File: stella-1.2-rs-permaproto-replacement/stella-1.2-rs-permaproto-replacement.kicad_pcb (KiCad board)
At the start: 2 copper layers, 81 x 51 mm, 10 parts, among them J1 Conn_01x03, J2 Conn_01x04, U1 Triad, U2 Humidity, U3 Surface Temp, U4 Range

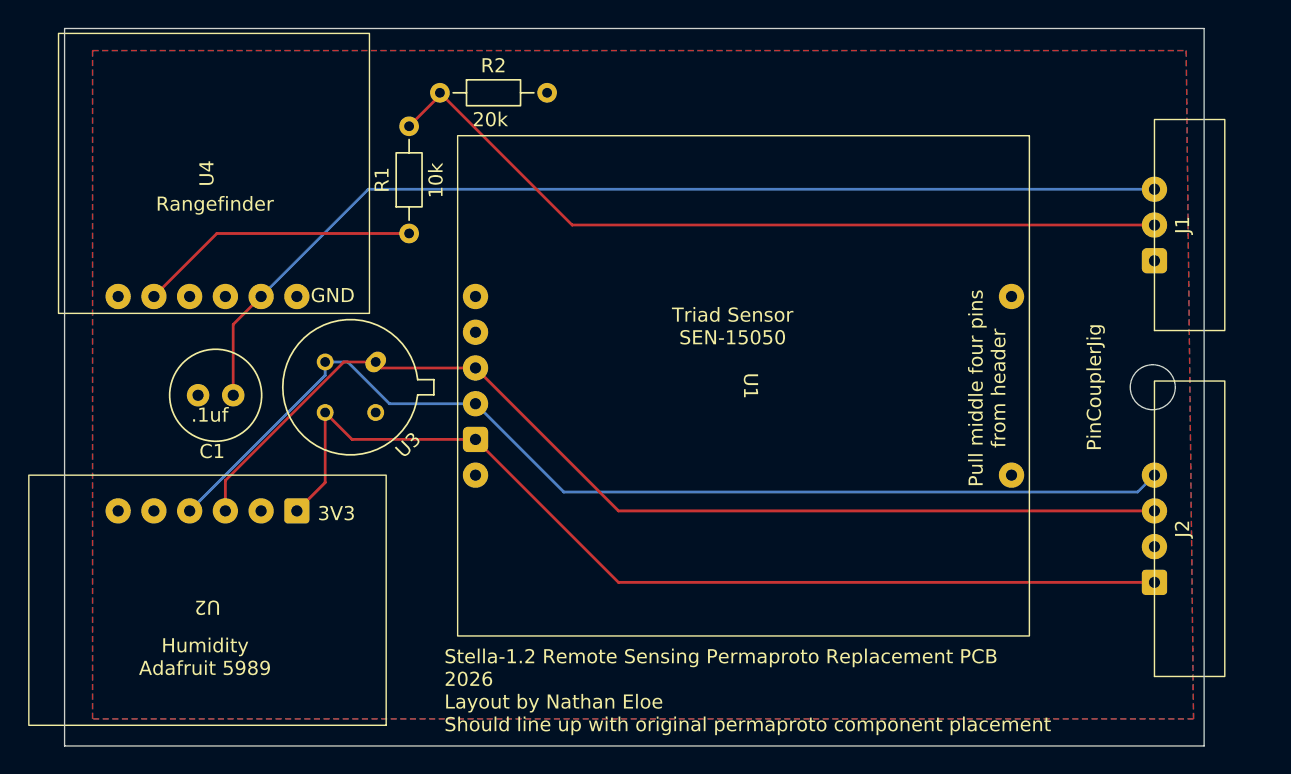
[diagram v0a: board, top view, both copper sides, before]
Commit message: Add RS build fixes (size, pins)
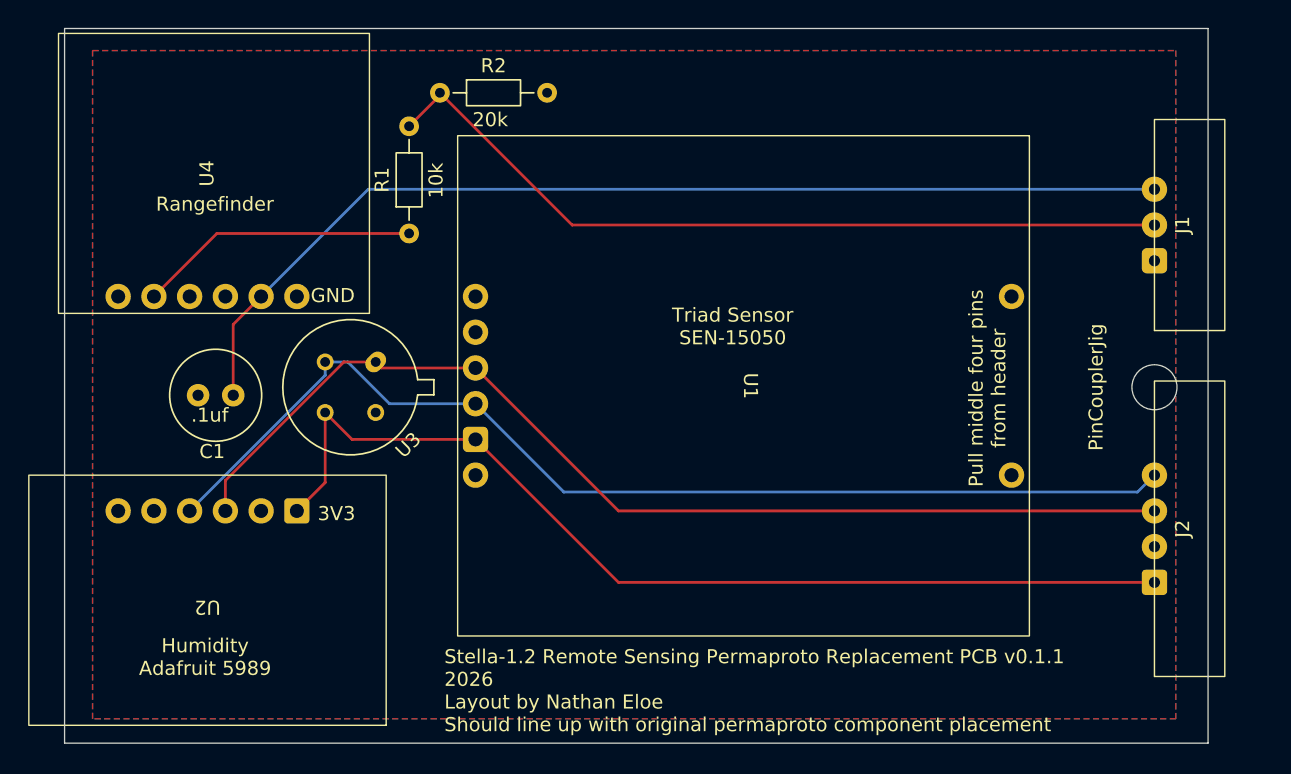
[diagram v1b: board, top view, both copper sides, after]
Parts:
- moved PinCouplerJig 0.12 mm to (157.5, 100.4)
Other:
- board size 81 x 51 mm -> 81.3 x 50.8 mm
- board text added: "Stella-1.2 Remote Sensing Permaproto Replacement PCB v0.1.1 2026 Layout by Nathan Eloe Should line up with original permaproto component placement"
- board text removed: "Stella-1.2 Remote Sensing Permaproto Replacement PCB 2026 Layout by Nathan Eloe Should line up with original permaproto component placement"
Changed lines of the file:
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@@
 		(sheetname "/")
 		(sheetfile "stella-1.2-rs-permaproto-replacement.kicad_sch")
-		(units
-			(unit
-				(name "A")
-				(pins "6" "5" "4" "3" "2" "1" "9" "8" "7")
-			)
-		)
 		(attr smd)
 		(duplicate_pad_numbers_are_jumpers no)
@@
 			(at -6.35 -19.05 270)
 			(size 1.8 1.8)
-			(drill 0.8)
+			(drill 1)
 			(layers "*.Cu" "*.Mask")
 			(remove_unused_layers no)
@@
 			(at 6.35 19.05 270)
 			(size 1.8 1.8)
-			(drill 0.8)
+			(drill 1)
 			(layers "*.Cu" "*.Mask")
 			(remove_unused_layers no)
@@
 			(at 3.81 19.05 270)
 			(size 1.8 1.8)
-			(drill 0.8)
+			(drill 1)
 			(layers "*.Cu" "*.Mask")
 			(remove_unused_layers no)
@@
 			(at 1.27 19.05 270)
 			(size 1.8 1.8)
-			(drill 0.8)
+			(drill 1)
 			(layers "*.Cu" "*.Mask")
 			(remove_unused_layers no)
@@
 			(at -1.27 19.05 270)
 			(size 1.8 1.8)
-			(drill 0.8)
+			(drill 1)
 			(layers "*.Cu" "*.Mask")
 			(remove_unused_layers no)
@@
 			(at -3.81 19.05 270)
 			(size 1.8 1.8)
-			(drill 0.8)
+			(drill 1)
 			(layers "*.Cu" "*.Mask")
 			(remove_unused_layers no)
@@
 			(at -6.35 19.05 270)
 			(size 1.8 1.8)
-			(drill 0.8)
+			(drill 1)
 			(layers "*.Cu" "*.Mask")
 			(remove_unused_layers no)
@@
 			(at 6.35 -19.05 270)
 			(size 1.8 1.8)
-			(drill 0.8)
+			(drill 1)
 			(layers "*.Cu" "*.Mask")
 			(remove_unused_layers no)
@@
 			(at -8.75 -6.81 90)
 			(size 1.8 1.8)
-			(drill 0.8)
+			(drill 1)
 			(layers "*.Cu" "*.Mask")
 			(remove_unused_layers no)
@@
 			(at -8.75 -4.27 90)
 			(size 1.8 1.8)
-			(drill 0.8)
+			(drill 1)
 			(layers "*.Cu" "*.Mask")
 			(remove_unused_layers no)
@@
 			(at -8.75 -1.73 90)
 			(size 1.8 1.8)
-			(drill 0.8)
+			(drill 1)
 			(layers "*.Cu" "*.Mask")
 			(remove_unused_layers no)
@@
 			(at -8.75 0.81 90)
 			(size 1.8 1.8)
-			(drill 0.8)
+			(drill 1)
 			(layers "*.Cu" "*.Mask")
 			(remove_unused_layers no)
@@
 			(at -8.75 3.35 90)
 			(size 1.8 1.8)
-			(drill 0.8)
+			(drill 1)
 			(layers "*.Cu" "*.Mask")
 			(remove_unused_layers no)
@@
 			(at -8.75 5.89 90)
 			(size 1.8 1.8)
-			(drill 0.8)
+			(drill 1)
 			(layers "*.Cu" "*.Mask")
 			(remove_unused_layers no)
@@
 		(sheetname "/")
 		(sheetfile "stella-1.2-rs-permaproto-replacement.kicad_sch")
-		(units
-			(unit
-				(name "A")
-				(pins "1" "2" "3" "4" "5" "6")
-			)
-		)
 		(attr smd)
 		(duplicate_pad_numbers_are_jumpers no)
@@
 			(at -6.35 6.35 180)
 			(size 1.8 1.8)
-			(drill 0.8)
+			(drill 1)
 			(layers "*.Cu" "*.Mask")
 			(remove_unused_layers no)
@@
 			(at -3.81 6.35 180)
 			(size 1.8 1.8)
-			(drill 0.8)
+			(drill 1)
 			(layers "*.Cu" "*.Mask")
 			(remove_unused_layers no)
@@
 			(at -1.27 6.35 180)
 			(size 1.8 1.8)
-			(drill 0.8)
+			(drill 1)
 			(layers "*.Cu" "*.Mask")
 			(remove_unused_layers no)
@@
 			(at 1.27 6.35 180)
 			(size 1.8 1.8)
-			(drill 0.8)
+			(drill 1)
 			(layers "*.Cu" "*.Mask")
 			(remove_unused_layers no)
@@
 			(at 3.81 6.35 180)
 			(size 1.8 1.8)
-			(drill 0.8)
+			(drill 1)
 			(layers "*.Cu" "*.Mask")
 			(remove_unused_layers no)
@@
 			(at 6.35 6.35 180)
 			(size 1.8 1.8)
-			(drill 0.8)
+			(drill 1)
 			(layers "*.Cu" "*.Mask")
 			(remove_unused_layers no)
@@
 	(footprint "MountingHole:MountingHole_3.2mm_M3"
 		(layer "F.Cu")
-		(at 157.36 100.43 90)
+		(at 157.48 100.43 90)
 		(descr "Mounting Hole 3.2mm, M3, no annular, generated by kicad-footprint-generator mountinghole.py")
 		(tags "mountinghole M3")
@@
 	(gr_rect
 		(start 80.01 74.93)
-		(end 161.01 125.93)
+		(end 161.29 125.73)
 		(radius 2.5)
 		(stroke
@@
 		)
 	)
-	(gr_text "Stella-1.2 Remote Sensing Permaproto Replacement PCB\n2026\nLayout by Nathan Eloe\nShould line up with original permaproto component placement"
+	(gr_text "Stella-1.2 Remote Sensing Permaproto Replacement PCB v0.1.1\n2026\nLayout by Nathan Eloe\nShould line up with original permaproto component placement"
 		(at 107 125 0)
 		(layer "F.SilkS")
@@
 		(layers "F.Cu" "B.Cu")
 		(hatch edge 0.5)
-		(connect_pads yes
+		(connect_pads thru_hole_only
 			(clearance 0.5)
 		)
@@
 		(polygon
 			(pts
-				(xy 82 76.5) (xy 159.736264 76.5) (xy 160.258242 124) (xy 82 124)
-			)
-		)
+				(xy 82 76.5) (xy 159 76.5) (xy 159 124) (xy 82 124)
+			)
+		)

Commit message: Add Adafruit AS7343 footprint to rs board
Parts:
- moved PinCouplerJig 0.10 mm to (157.5, 100.3)
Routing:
- net +3V3: track 71.8 -> 80.2 mm
- net /I2C_SCL: track 76.1 -> 79.6 mm
- net /I2C_SDA: track 77.8 -> 76.9 mm
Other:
- board text added: "Spectral Sensor"
- board text removed: "Triad Sensor SEN-15050"
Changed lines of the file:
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@@
 		(sheetname "/")
 		(sheetfile "stella-1.2-rs-permaproto-replacement.kicad_sch")
+		(units
+			(unit
+				(name "A")
+				(pins "6" "5" "4" "3" "2" "1" "9" "8" "7")
+			)
+		)
 		(attr smd)
 		(duplicate_pad_numbers_are_jumpers no)
 		(fp_rect
+			(start -12.7 -8.89)
+			(end 12.7 8.89)
+			(radius 2.54)
+			(stroke
+				(width 0.1)
+				(type solid)
+			)
+			(fill no)
+			(layer "F.SilkS")
+		)
+		(fp_rect
 			(start -17.77995 -20.31995)
 			(end 17.77995 20.31995)
+			(radius 2.54)
 			(stroke
 				(width 0.1)
@@
 			(fill no)
 			(layer "F.SilkS")
+		)
+		(fp_text user "SEN-15050"
+			(at -16.5 20 270)
+			(unlocked yes)
+			(layer "F.SilkS")
+			(effects
+				(font
+					(size 1 1)
+					(thickness 0.1)
+				)
+				(justify left bottom)
+			)
+		)
+		(fp_text user "3v3"
+			(at 2.5 17.5 270)
+			(unlocked yes)
+			(layer "F.SilkS")
+			(effects
+				(font
+					(size 1 1)
+					(thickness 0.1)
+				)
+				(justify left bottom)
+			)
+		)
+		(fp_text user "Adafruit 6477 (AS7343)"
+			(at -9 -6.5 270)
+			(unlocked yes)
+			(layer "F.SilkS")
+			(effects
+				(font
+					(size 1 1)
+					(thickness 0.1)
+				)
+				(justify left bottom)
+			)
+		)
+		(fp_text user "Remove middle 4 pins"
+			(at -8.5 -16.5 270)
+			(unlocked yes)
+			(layer "F.SilkS")
+			(effects
+				(font
+					(size 1 1)
+					(thickness 0.1)
+				)
+				(justify left bottom)
+			)
 		)
 		(fp_text user "${REFERENCE}"
@@
 		)
 		(pad "1" thru_hole circle
-			(at 6.35 19.05 270)
+			(at -3.81 6.35 270)
 			(size 1.8 1.8)
 			(drill 1)
@@
 			(net "GND")
 			(pinfunction "GND_1")
+			(pintype "power_in")
+		)
+		(pad "1" thru_hole circle
+			(at 6.35 19.05 270)
+			(size 1.8 1.8)
+			(drill 1)
+			(layers "*.Cu" "*.Mask")
+			(remove_unused_layers no)
+			(net "GND")
+			(pinfunction "GND_1")
+			(pintype "power_in")
+		)
+		(pad "2" thru_hole roundrect
+			(at -6.35 6.35 270)
+			(size 1.8 1.8)
+			(drill 1)
+			(layers "*.Cu" "*.Mask")
+			(remove_unused_layers no)
+			(roundrect_rratio 0.1388888889)
+			(net "+3V3")
+			(pinfunction "3v3_2")
 			(pintype "power_in")
 		)
@@
 		)
 		(pad "3" thru_hole circle
-			(at 1.27 19.05 270)
+			(at 1.27 6.35 270)
 			(size 1.8 1.8)
 			(drill 1)
@@
 			(pintype "bidirectional")
 		)
+		(pad "3" thru_hole circle
+			(at 1.27 19.05 270)
+			(size 1.8 1.8)
+			(drill 1)
+			(layers "*.Cu" "*.Mask")
+			(remove_unused_layers no)
+			(net "/I2C_SDA")
+			(pinfunction "SDA_3")
+			(pintype "bidirectional")
+		)
 		(pad "4" thru_hole circle
-			(at -1.27 19.05 270)
+			(at -1.27 6.35 270)
 			(size 1.8 1.8)
 			(drill 1)
@@
 			(pintype "bidirectional")
 		)
+		(pad "4" thru_hole circle
+			(at -1.27 19.05 270)
+			(size 1.8 1.8)
+			(drill 1)
+			(layers "*.Cu" "*.Mask")
+			(remove_unused_layers no)
+			(net "/I2C_SCL")
+			(pinfunction "SCL_4")
+			(pintype "bidirectional")
+		)
 		(pad "5" thru_hole circle
 			(at -3.81 19.05 270)
@@
 			(pintype "output+no_connect")
 		)
+		(pad "5" thru_hole circle
+			(at 3.81 6.35 270)
+			(size 1.8 1.8)
+			(drill 1)
+			(layers "*.Cu" "*.Mask")
+			(remove_unused_layers no)
+			(net "unconnected-(U1-~{INT}-Pad5)_1")
+			(pinfunction "~{INT}_5")
+			(pintype "output+no_connect")
+		)
 		(pad "6" thru_hole circle
 			(at -6.35 19.05 270)
+			(size 1.8 1.8)
+			(drill 1)
+			(layers "*.Cu" "*.Mask")
+			(remove_unused_layers no)
+			(net "unconnected-(U1-~{RST}-Pad6)_1")
+			(pinfunction "~{RST}_6")
+			(pintype "input+no_connect")
+		)
+		(pad "6" thru_hole circle
+			(at 6.35 6.35 270)
 			(size 1.8 1.8)
 			(drill 1)
@@
 		(sheetname "/")
 		(sheetfile "stella-1.2-rs-permaproto-replacement.kicad_sch")
+		(units
+			(unit
+				(name "A")
+				(pins "3" "2" "1" "7" "6" "5" "4")
+			)
+		)
 		(attr smd)
 		(duplicate_pad_numbers_are_jumpers no)
@@
 		(sheetname "/")
 		(sheetfile "stella-1.2-rs-permaproto-replacement.kicad_sch")
+		(units
+			(unit
+				(name "A")
+				(pins "1" "2" "3" "4" "5" "6")
+			)
+		)
 		(attr smd)
 		(duplicate_pad_numbers_are_jumpers no)
@@
 	(footprint "MountingHole:MountingHole_3.2mm_M3"
 		(layer "F.Cu")
-		(at 157.48 100.43 90)
+		(at 157.48 100.33 90)
 		(descr "Mounting Hole 3.2mm, M3, no annular, generated by kicad-footprint-generator mountinghole.py")
 		(tags "mountinghole M3")
@@
 		)
 		(pad "" np_thru_hole circle
-			(at 0 0 90)
+			(at 0 0)
 			(size 3.2 3.2)
 			(drill 3.2)
@@
 		)
 	)
-	(gr_text "Triad Sensor\nSEN-15050"
-		(at 127.5 97.5 0)
+	(gr_text "Spectral Sensor"
+		(at 128 86.5 0)
 		(layer "F.SilkS")
 		(effects
@@
 	)
 	(segment
+		(start 151.557057 99.06)
+		(end 121.92 99.06)
+		(width 0.2)
+		(layer "F.Cu")
+		(net "/I2C_SCL")
+	)
+	(segment
+		(start 158.68 108.02)
+		(end 158.68 106.182943)
+		(width 0.2)
+		(layer "F.Cu")
+		(net "/I2C_SCL")
+	)
+	(segment
 		(start 102.552102 99.06)
 		(end 102.126051 98.633949)
@@
 	)
 	(segment
-		(start 119.38 109.22)
-		(end 109.22 99.06)
-		(width 0.2)
-		(layer "F.Cu")
-		(net "/I2C_SCL")
-	)
-	(segment
 		(start 99.866051 98.633949)
 		(end 91.44 107.06)
@@
 	(segment
 		(start 157.48 109.22)
-		(end 119.38 109.22)
+		(end 158.68 108.02)
 		(width 0.2)
 		(layer "F.Cu")
@@
 	)
 	(segment
+		(start 109.22 99.06)
+		(end 121.92 99.06)
+		(width 0.2)
+		(layer "F.Cu")
+		(net "/I2C_SCL")
+	)
+	(segment
 		(start 102.126051 98.633949)
 		(end 99.866051 98.633949)
@@
 	)
 	(segment
+		(start 158.68 106.182943)
+		(end 151.557057 99.06)
+		(width 0.2)
+		(layer "F.Cu")
+		(net "/I2C_SCL")
+	)
+	(segment
 		(start 157.48 106.68)
-		(end 156.28 107.88)
+		(end 152.4 101.6)
+		(width 0.2)
+		(layer "F.Cu")
+		(net "/I2C_SDA")
+	)
+	(segment
+		(start 152.4 101.6)
+		(end 121.92 101.6)
+		(width 0.2)
+		(layer "F.Cu")
+		(net "/I2C_SDA")
+	)
+	(segment
+		(start 109.22 101.6)
+		(end 121.92 101.6)
+		(width 0.2)
+		(layer "F.Cu")
+		(net "/I2C_SDA")
+	)
+	(segment
+		(start 98.533949 99.586051)
+		(end 88.9 109.22)
 		(width 0.2)
 		(layer "B.Cu")
@@
 	)
 	(segment
-		(start 98.533949 99.586051)
-		(end 88.9 109.22)
+		(start 103.1 101.6)
+		(end 100.133949 98.633949)
 		(width 0.2)
 		(layer "B.Cu")
@@
 	)
 	(segment
-		(start 103.1 101.6)
-		(end 100.133949 98.633949)
+		(start 100.133949 98.633949)
+		(end 98.533949 98.633949)
 		(width 0.2)
 		(layer "B.Cu")
@@
 	)
 	(segment
-		(start 115.5 107.88)
-		(end 109.22 101.6)
+		(start 109.22 101.6)
+		(end 103.1 101.6)
 		(width 0.2)
 		(layer "B.Cu")
@@
 	)
 	(segment
-		(start 156.28 107.88)
-		(end 115.5 107.88)
+		(start 98.533949 98.633949)
+		(end 98.533949 99.586051)
 		(width 0.2)
 		(layer "B.Cu")
@@
 	)
 	(segment
-		(start 100.133949 98.633949)
-		(end 98.533949 98.633949)
-		(width 0.2)
-		(layer "B.Cu")
-		(net "/I2C_SDA")
-	)
-	(segment
-		(start 109.22 101.6)
-		(end 103.1 101.6)
-		(width 0.2)
-		(layer "B.Cu")
-		(net "/I2C_SDA")
-	)
-	(segment
-		(start 98.533949 98.633949)
-		(end 98.533949 99.586051)
-		(width 0.2)
-		(layer "B.Cu")
-		(net "/I2C_SDA")
-	)
-	(segment
-		(start 119.38 114.3)
-		(end 109.22 104.14)
-		(width 0.2)
-		(layer "F.Cu")
-		(net "+3V3")
-	)
-	(segment
 		(start 98.533949 102.226051)
 		(end 98.533949 107.206051)
@@
 	)
 	(segment
-		(start 157.48 114.3)
-		(end 119.38 114.3)
-		(width 0.2)
-		(layer "F.Cu")
-		(net "+3V3")
-	)
-	(segment
 		(start 98.533949 107.206051)
 		(end 96.52 109.22)
@@
 		(net "+3V3")
 	)
+	(segment
+		(start 121.92 93.98)
+		(end 121.52 93.98)
+		(width 0.2)
+		(layer "B.Cu")
+		(net "+3V3")
+	)
+	(segment
+		(start 111.36 104.14)
+		(end 109.22 104.14)
+		(width 0.2)
+		(layer "B.Cu")
+		(net "+3V3")
+	)
+	(segment
+		(start 142.24 114.3)
+		(end 121.92 93.98)
+		(width 0.2)
+		(layer "B.Cu")
+		(net "+3V3")
+	)
+	(segment
+		(start 121.52 93.98)
+		(end 111.36 104.14)
+		(width 0.2)
+		(layer "B.Cu")
+		(net "+3V3")
+	)
+	(segment
+		(start 157.48 114.3)
+		(end 142.24 114.3)
+		(width 0.2)
+		(layer "B.Cu")
+		(net "+3V3")
+	)
